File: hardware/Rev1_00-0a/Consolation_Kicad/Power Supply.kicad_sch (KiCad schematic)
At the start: 55 parts, among them Q1 SSM3K56FS,LF, Q2 SSM3K56FS,LF, Q3 SSM3K56FS,LF, U10 TPS62826DMQR, U7 TPS79901DRVR, U9 TPS61230ARNSR

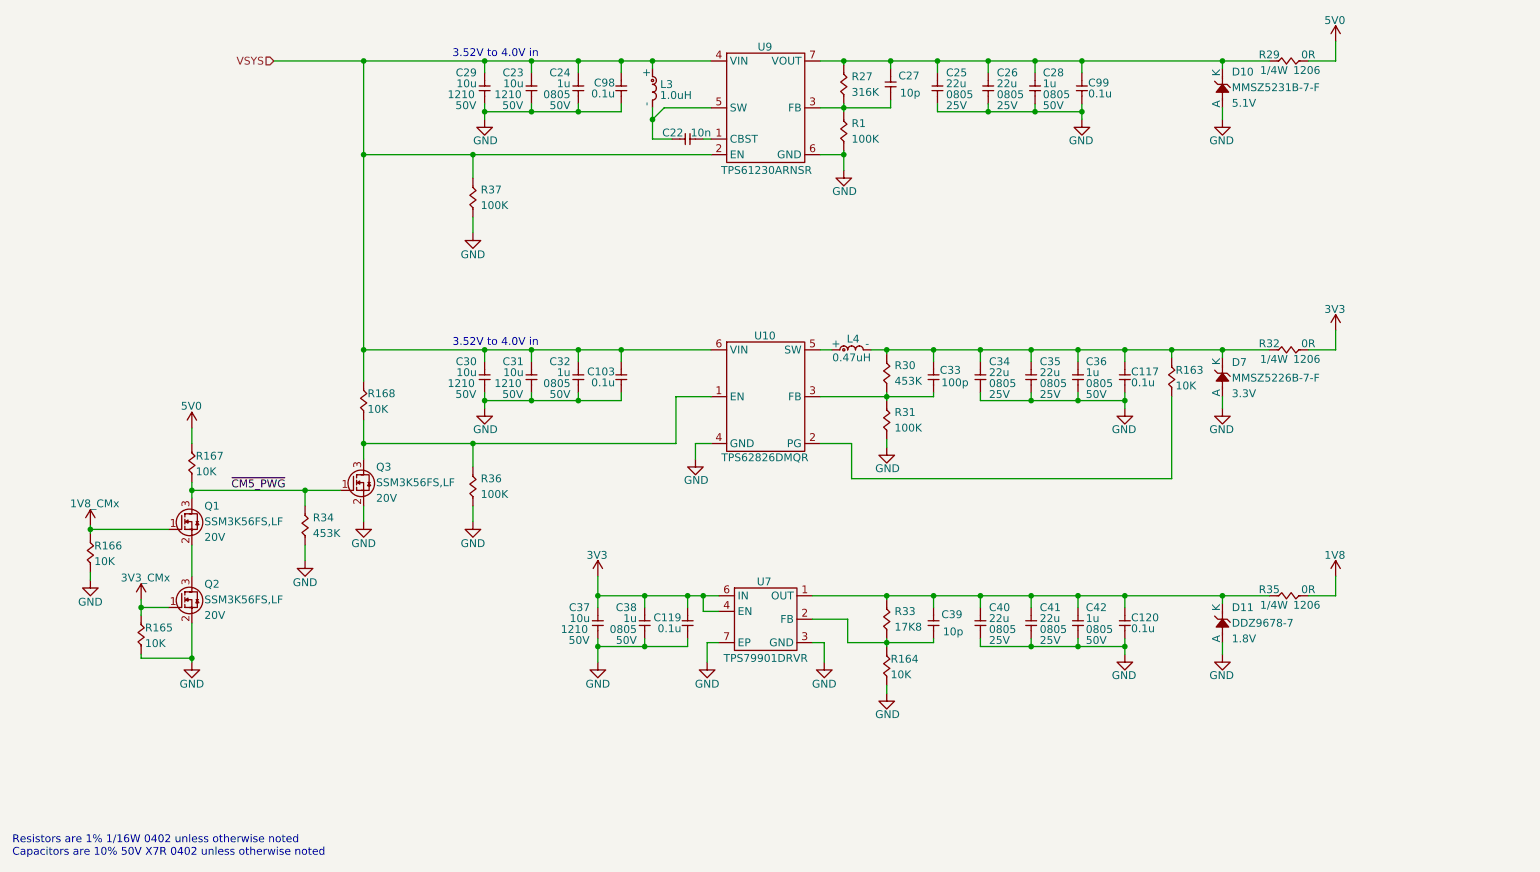
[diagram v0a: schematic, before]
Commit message: Removed unnecessary functions (USB2 mux, CapTouch) Adjusted 220uF alum capacitor for codec (slimmer version)
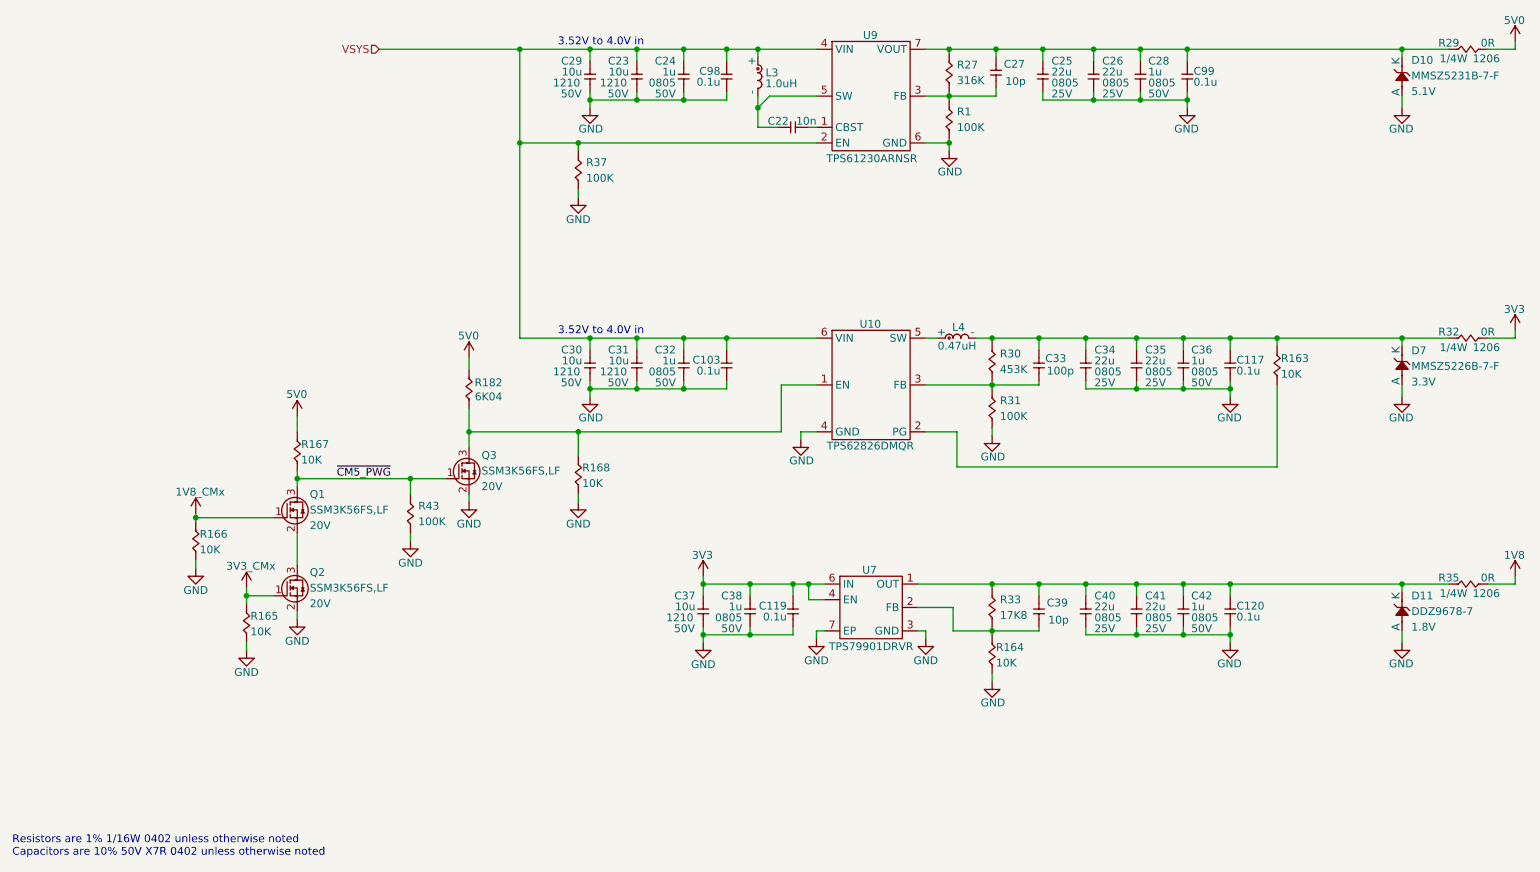
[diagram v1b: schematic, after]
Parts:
- removed R34: 453K, footprint:RES_0402, symbol KicadCompDb:Resistors/RES_SMT_00039
- removed R36: 100K, footprint:RES_0402, symbol KicadCompDb:Resistors/RES_SMT_00018
- added R182: 6K04, footprint:RES_0402, symbol KicadCompDb:Resistors/RES_SMT_00011
- added R43: 100K, footprint:RES_0402, symbol KicadCompDb:Resistors/RES_SMT_00018
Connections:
- net 5V0: now also R182.2
- net GND: now also R168.1, R43.1
- net VSYS: no longer R168.2
- net ~{CM5_PWG}: now also R43.2
- net at Q3.3 (D), U10.1 (EN): now also R168.2, R182.1; no longer R168.1
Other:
- moved on the sheet: C103, C117, C119, C120, C22, C23, C24, C25, C26, C27, C28, C29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

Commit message: Work on preliminary placement + RP2350A fanout
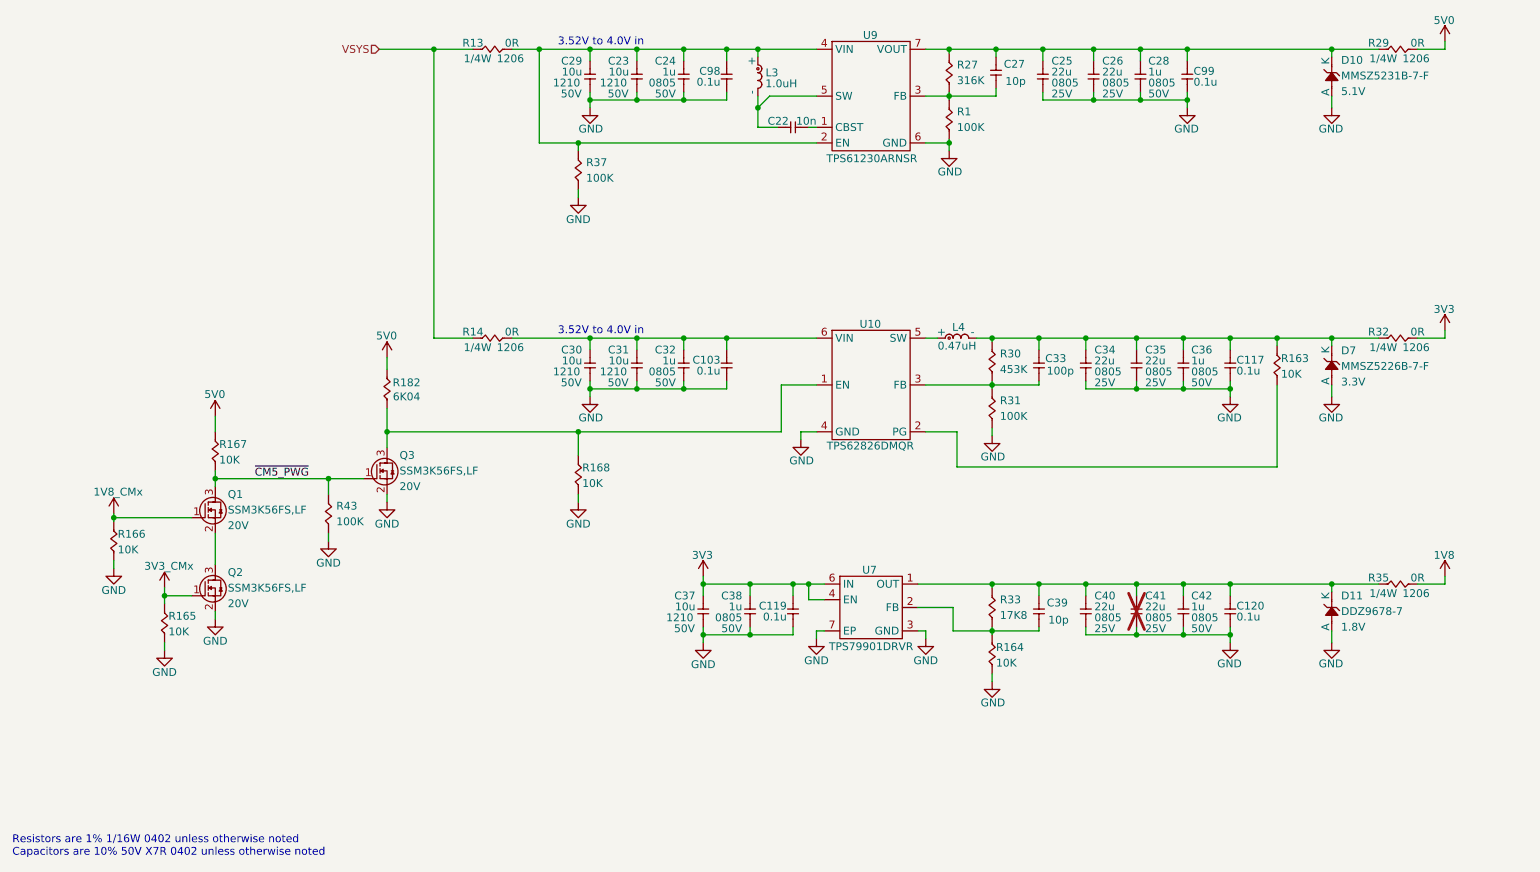
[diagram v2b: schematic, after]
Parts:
- added R13, R14: 0R, footprint:RES_1206, symbol KicadCompDb:Resistors/RES_SMT_00022
- C41: now not fitted
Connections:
- net VSYS: now also R13.1, R14.1; no longer C103.2, C23.2, C24.2, C29.2, C30.2, C31.2, C32.2, C98.2, L3.1 (+), R37.2, U10.6 (VIN), U9.2 (EN), U9.4 (VIN)
- new net: C23.2, C24.2, C29.2, C98.2, L3.1 (+), R13.2, R37.2, U9.2 (EN), U9.4 (VIN)
- new net: C103.2, C30.2, C31.2, C32.2, R14.2, U10.6 (VIN)
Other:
- moved on the sheet: D10, D11, D7, Q1, Q2, Q3, R165, R166, R167, R182, R29, R32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

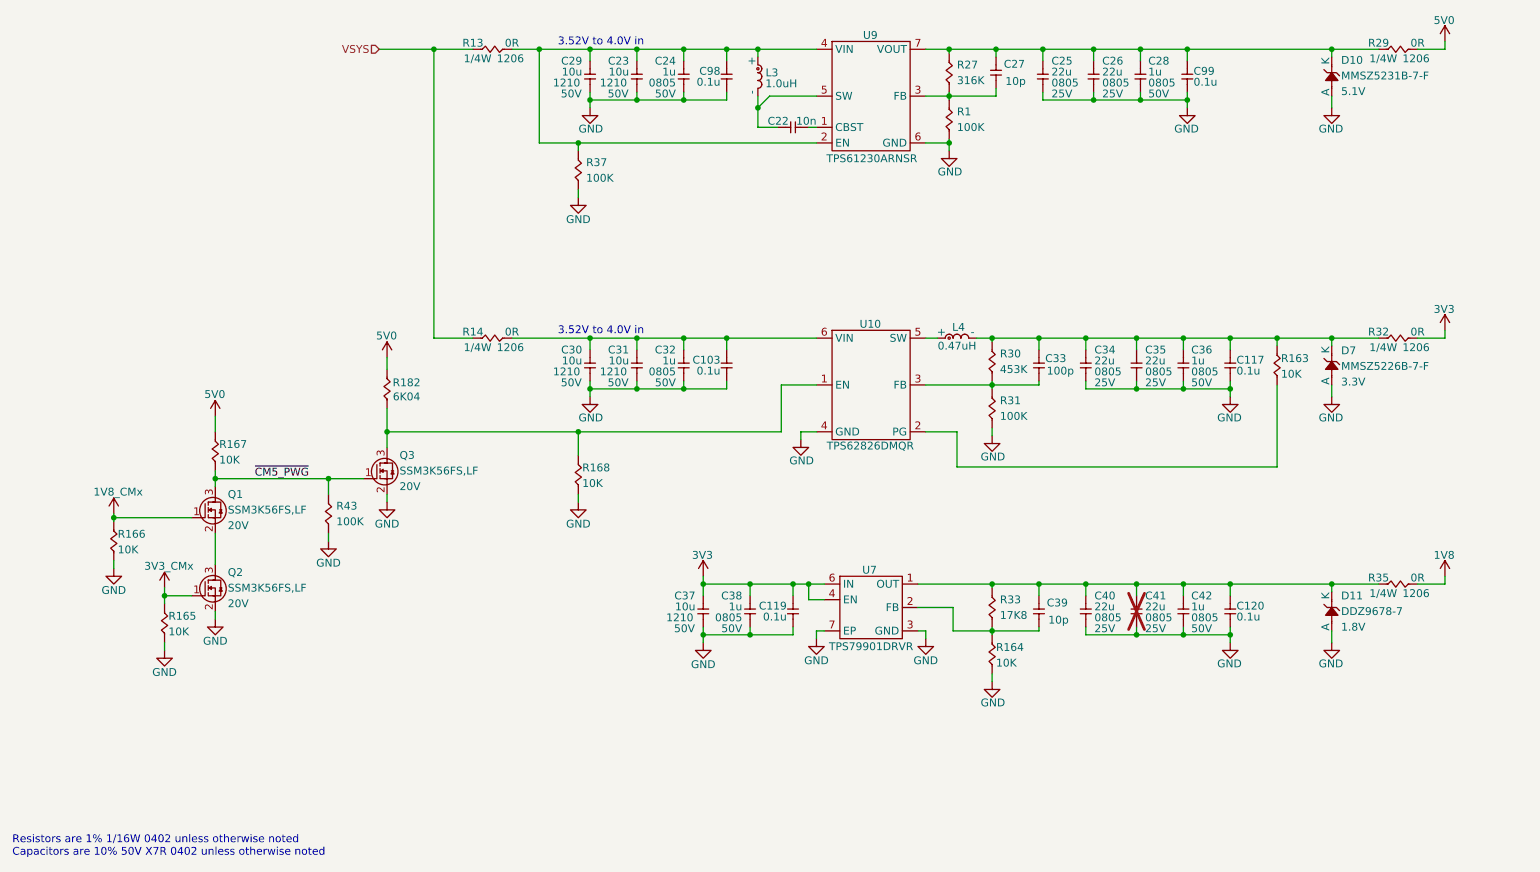
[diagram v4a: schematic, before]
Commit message: Preliminary placement done Add test points to PCB
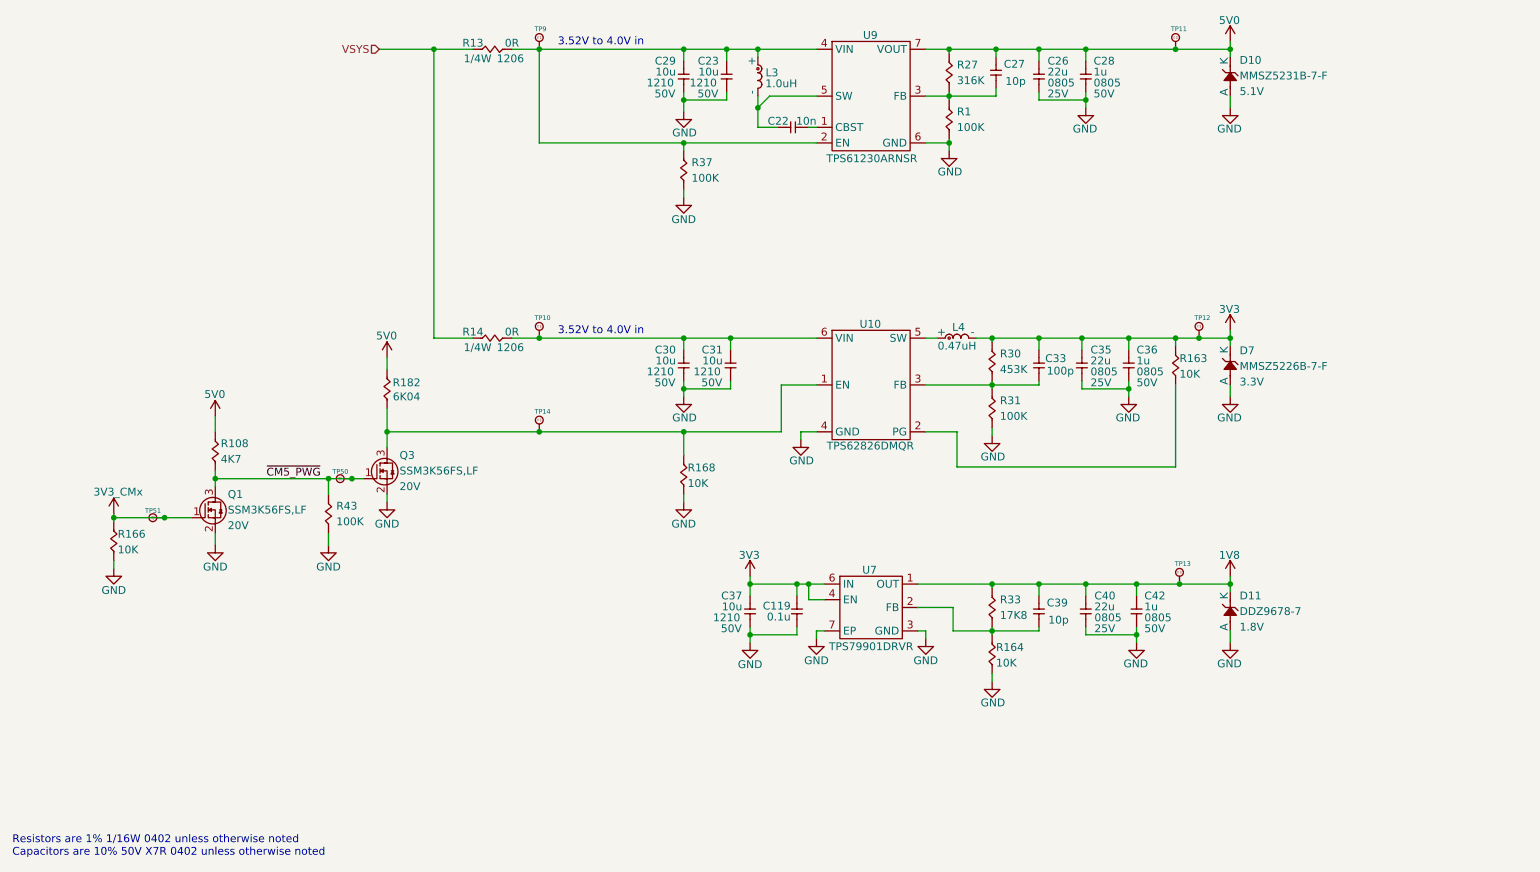
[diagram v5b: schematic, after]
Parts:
- removed C103, C117, C120, C98, C99: 0.1u, footprint:CAP_NONPOL_0402, symbol KicadCompDb:Capacitors/CAP_CER_SMT_00001
- removed C24, C32, C38: 1u, footprint:CAP_NONPOL_0805, symbol KicadCompDb:Capacitors/CAP_CER_SMT_00002
- removed C25, C34, C41: 22u, footprint:CAP_NONPOL_0805, symbol KicadCompDb:Capacitors/CAP_CER_SMT_00011
- removed Q2: SSM3K56FS,LF, footprint:SC-75, symbol KicadCompDb:Mosfet/MOSFET_00002
- removed R165, R167: 10K, footprint:RES_0402, symbol KicadCompDb:Resistors/RES_SMT_00013
- removed R29, R32, R35: 0R, footprint:RES_1206, symbol KicadCompDb:Resistors/RES_SMT_00022
- added R108: 4K7, footprint:RES_0402, symbol KicadCompDb:Resistors/RES_SMT_00010
- added TP10, TP11, TP12, TP13, TP14, TP50, TP51, TP9: 75 mils, footprint:SMT_TP_75_MILS, symbol KicadCompDb:Test Point/TP_00004
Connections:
- net 1V8_CMx is gone; now on net 3V3_CMx: Q1.1 (G), R166.2
- net 1V8: now also C39.2, C40.2, C42.2, D11.1 (K), R33.2, U7.1 (OUT), TP13.1
- net 3V3: now also C33.2, C35.2, C36.2, D7.1 (K), L4.2 (-), R163.2, R30.2, TP12.1
- net 3V3_CMx: now also TP51.1
- net 5V0: now also C26.2, C27.2, C28.2, D10.1 (K), R27.2, U9.7 (VOUT), R108.2, TP11.1
- net GND: now also Q1.2 (S)
- net ~{CM5_PWG}: now also R108.1, TP50.1
- net at C23.2, C29.2, L3.1 (+)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: now also TP9.1
- net at Q3.3 (D), R168.2, R182.1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: now also TP14.1
- net at C30.2, C31.2, R14.2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: now also TP10.1
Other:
- moved on the sheet: C119, C23, C26, C28, C29, C30, C31, C35, C36, C37, C42, D10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
